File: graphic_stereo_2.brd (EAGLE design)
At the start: 109 x 29.5 mm, 82 parts, among them IC1 NE5532D, IC2 NE5532D, IC3 NE5532D, IC4 NE5532D, IC5 NE5532D

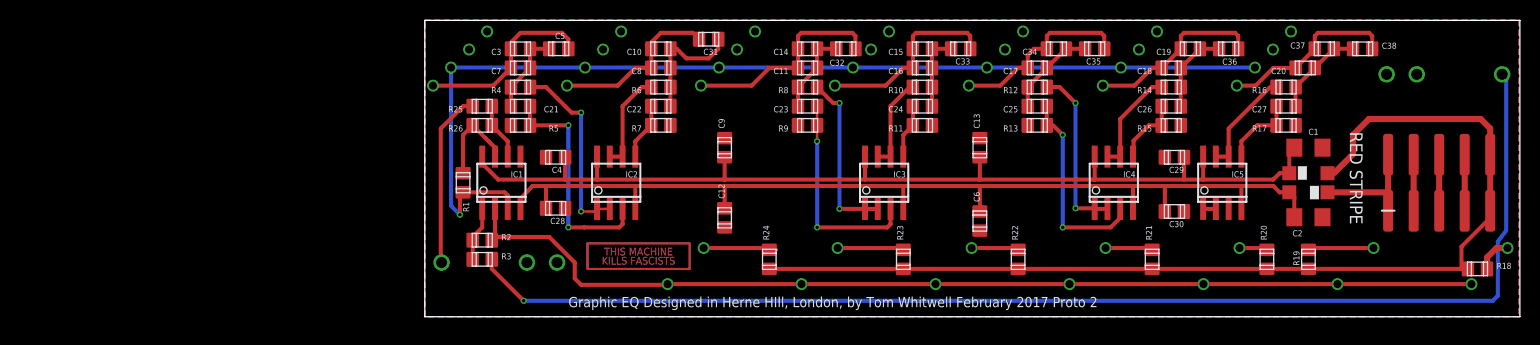
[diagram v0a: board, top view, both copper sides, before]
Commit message: Revert "Merge branch 'fix-panel'"
This reverts commit 24303b16601d2e124062e02205cddf4c546a9bcf, reversing
changes made to eef96a0ff0da711b8061c4b766c52a963260b08f.
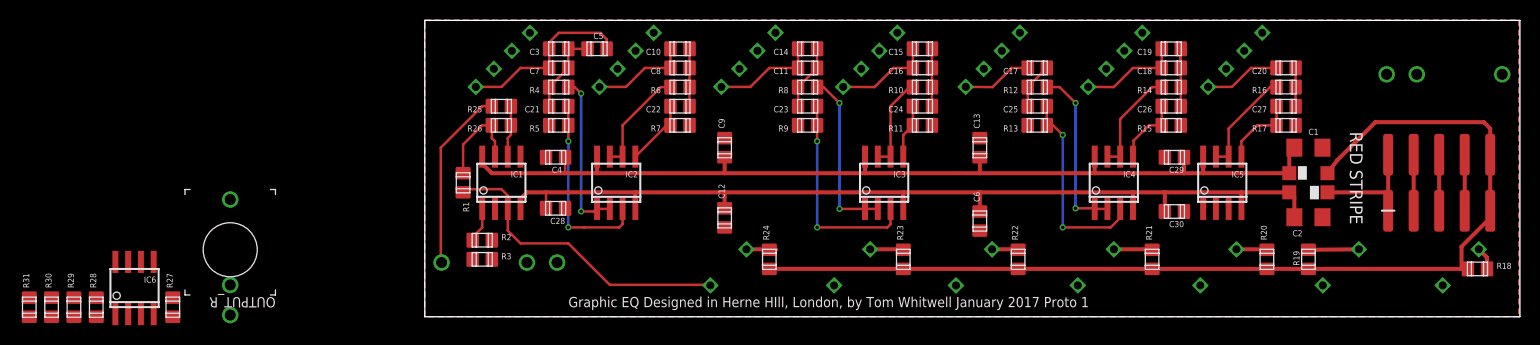
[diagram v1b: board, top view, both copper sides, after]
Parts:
- removed C31, C32, C33, C34, C35, C36, C37, C38: NP, we-rcl:C0805
- removed U$1: (no value), MusicThingModular:TMKF
- added IC6: NE5532D, linear:SO08
- added OUTPUT_R: THONKICONNNEW, MusicThingModular:WQP-PJ301M-12_JACK
- added R27, R28: 2.7k, we-rcl:C0805
- added R29, R30: 10k, we-rcl:C0805
- added R31: 470R, we-rcl:C0805
- 160HZ, 16KHZ, 1KHZ, 2.5KHZ, 410HZ, 63HZ, 7.7KHZ: device MusicThingModular:ALPHA_ILL_FADER_20MM_REV2 -> TomW:ALPHA_ILL_FADER_20MM
- R18, R19, R20, R21, R22, R23, R24: value 2k -> 470R
- moved 63HZ 4.26 mm to (18.5, 14.8)
- moved C21 3.81 mm to (13.3, 21.0)
- moved C3 3.81 mm to (13.3, 26.7)
- moved C7 3.81 mm to (13.3, 24.8)
- moved R4 3.81 mm to (13.3, 22.9)
- moved R5 3.81 mm to (13.3, 19.1)
- moved C5 3.81 mm to (17.1, 26.7)
- moved 160HZ 3.24 mm to (30.9, 14.8)
- moved 16KHZ 2.86 mm to (91.4, 14.8)
- moved 410HZ 2.04 mm to (43.0, 14.8)
- moved C19 1.91 mm to (74.3, 26.7)
- moved C20 1.91 mm to (85.7, 24.8)
- moved R25 1.91 mm to (7.62, 21.0)
- moved R26 1.91 mm to (7.62, 19.1)
- moved C10 1.90 mm to (25.4, 26.7)
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- renumbered OUTPUT to OUTPUTL/MONO
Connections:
- new net N$1: 160HZ.3, 1KHZ.3, 7.7KHZ.3, IC6.3, R27.1
- new net N$44: IC6.1, R28.2, R3.2
- new net N$46: 16KHZ.1, 2.5KHZ.1, 410HZ.1, 63HZ.1, IC1.2, R2.1
- new net N$47: IC5.3, R29.1, R30.1
- new net N$48: IC5.1, IC5.2, R31.2
- new net N$49: OUTPUTL/MONO.P$1_TIP, R31.1
- new net V+: IC6.8
- new net V-: IC6.4
- net GND: no longer IC5.3
- net N$11: no longer C34.1, C35.2
- net N$12: no longer C33.2
- net N$14: no longer C31.1
- net N$18: no longer C31.2
- net N$19: no longer C36.1
- net N$22: now also 160HZ.1, 1KHZ.1, 7.7KHZ.1, IC6.2, R28.1; no longer IC5.1, IC5.2
- net N$23: no longer C37.1, C38.1
- net N$3: now also IC1.3, R1.1; no longer 160HZ.3, 1KHZ.3, 7.7KHZ.3, IC1.2, R2.1
- net N$30: no longer C32.1
- net N$31: no longer C33.1
- net N$36: no longer C34.2, C35.1
- net N$37: no longer C36.2
- net N$4: no longer C32.2
- net N$40: no longer C37.2, C38.2
- net N$45: now also R27.2
- net N$5: now also R30.2; no longer R3.2
- net N$6: now also OUTPUT_R.P$1_TIP; no longer OUTPUTL/MONO.P$1_TIP
- net N$7: now also OUTPUT_R.P$2_SWITCH, R29.2; no longer 160HZ.1, 16KHZ.1, 1KHZ.1, 2.5KHZ.1, 410HZ.1, 63HZ.1, 7.7KHZ.1, IC1.3, R1.1
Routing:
- net N$6: track 125.1 -> 0.00 mm, vias 1 -> 0
- net N$7: track 103.3 -> 0.00 mm, vias 1 -> 0
- net N$3: track 103.4 -> 30.8 mm
- net N$11: track 18.5 -> 6.96 mm
- net N$4: track 20.8 -> 10.3 mm
- net N$23: track 17.8 -> 7.59 mm
- net N$12: track 18.9 -> 9.63 mm
- net N$19: track 17.8 -> 10.0 mm
- net N$14: track 17.1 -> 9.75 mm
- net -12V: track 101.0 -> 94.1 mm
- net N$18: track 12.2 -> 5.72 mm
- net +12V: track 103.2 -> 97.6 mm
- net N$40: track 9.20 -> 3.81 mm
- net N$36: track 9.20 -> 4.60 mm
- net N$25: track 22.9 -> 19.1 mm
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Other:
- board text added: "Graphic EQ Designed in Herne HIll, London, by Tom Whitwell January 2017 Proto 1"
- board text removed: "Graphic EQ Designed in Herne HIll, London, by Tom Whitwell February 2017 Proto 2"
